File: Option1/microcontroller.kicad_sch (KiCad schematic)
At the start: 15 parts, among them U801 ESP32-WROOM-32E-N4, U802 MCP23017_SO

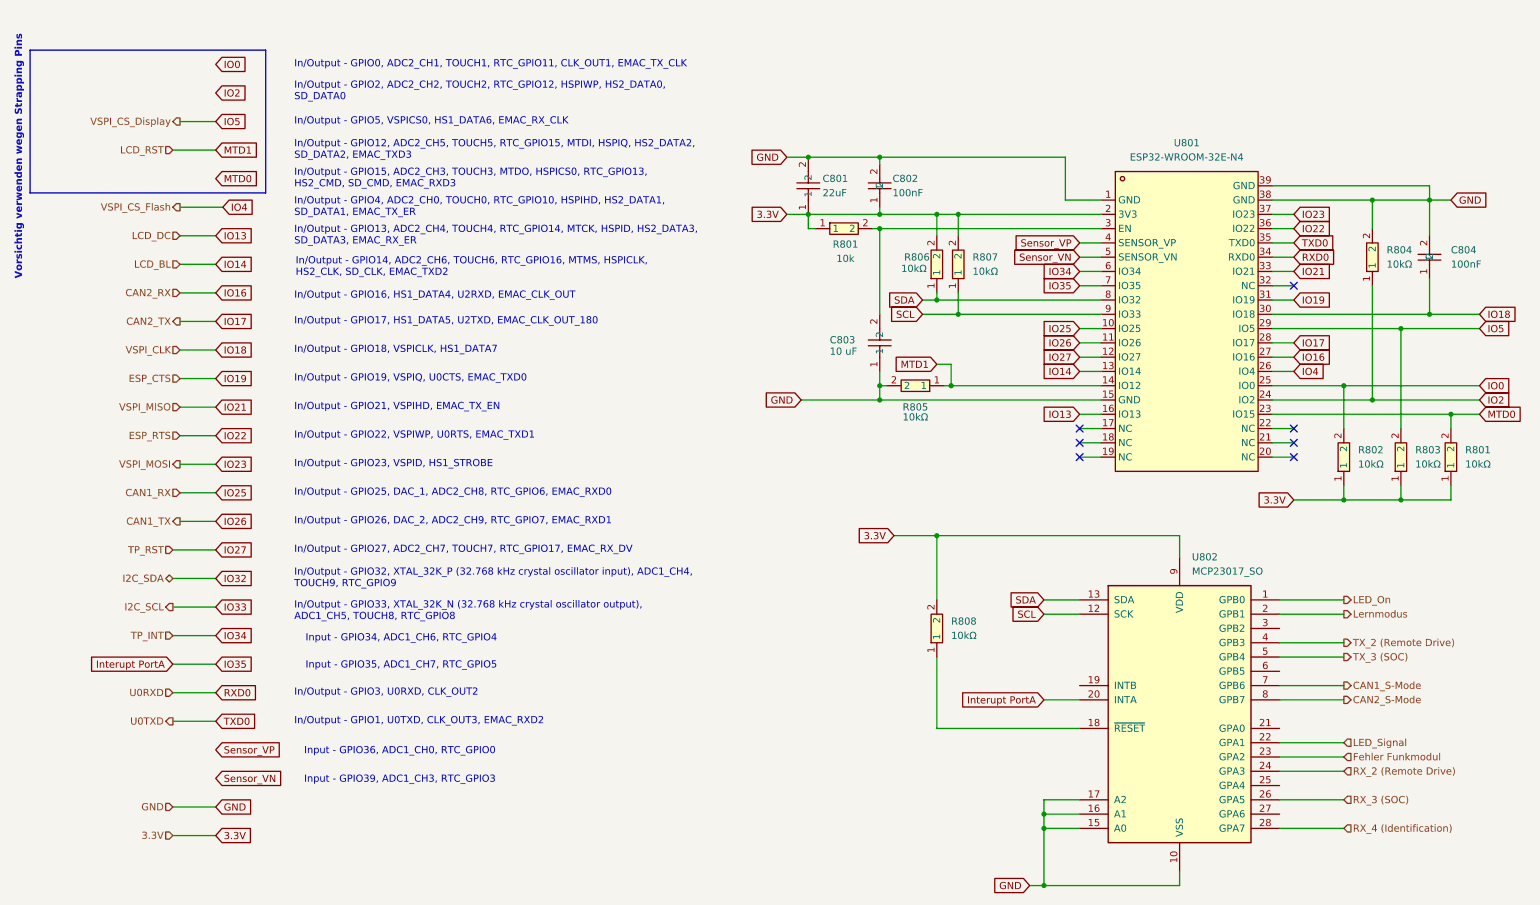
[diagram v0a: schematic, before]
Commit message: SPI Flash hinzugefügt, IN/Outputs vereinheitlicht, USB Flash Möglichkeit hinzugefügt, Display fehtl noch
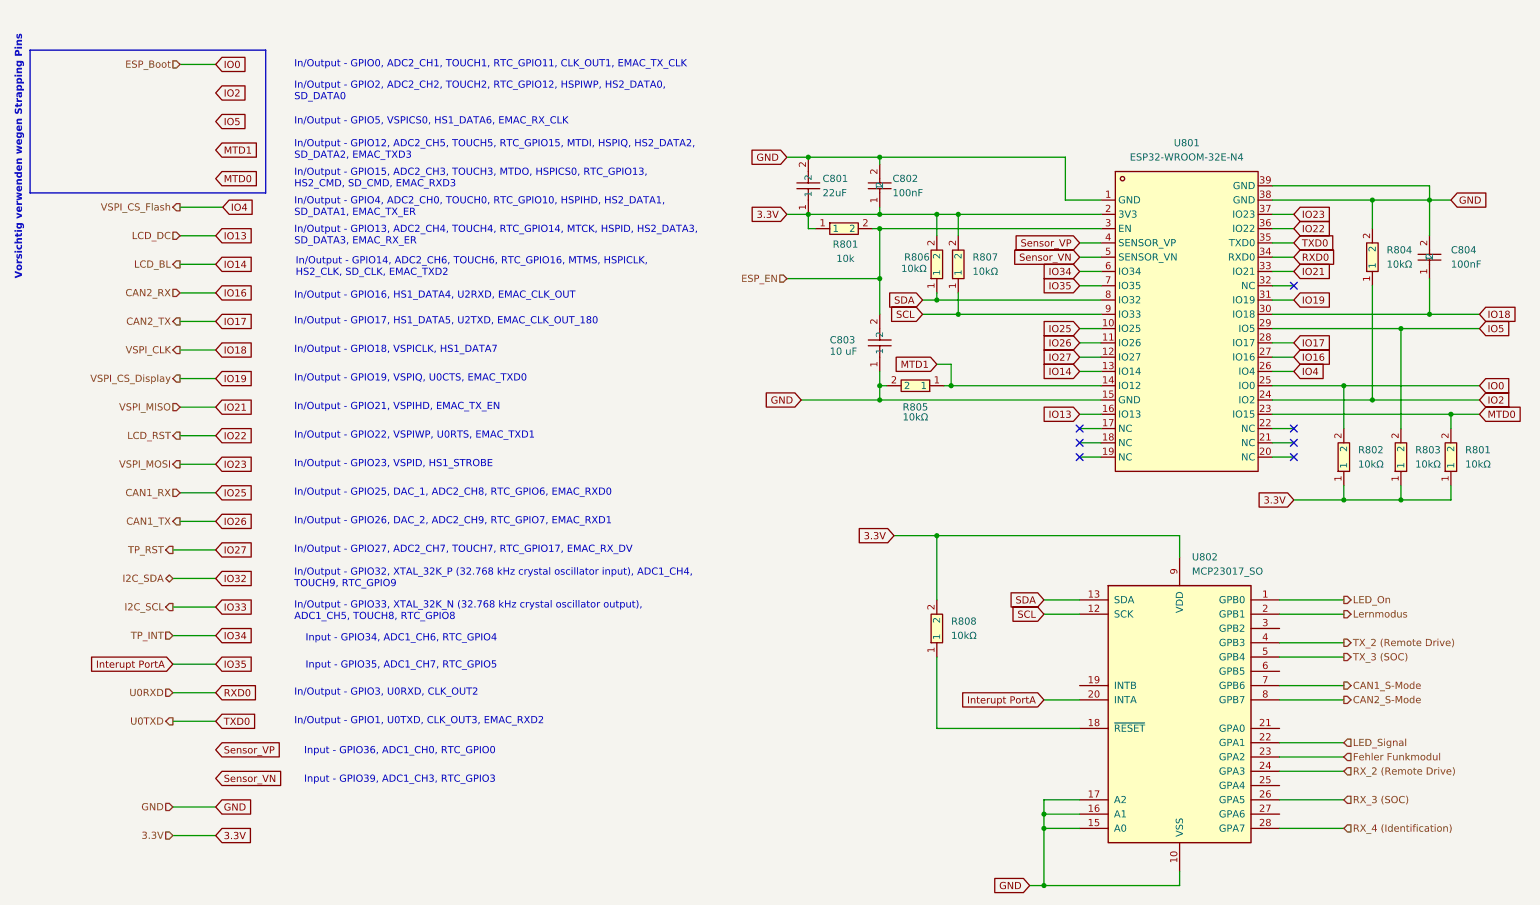
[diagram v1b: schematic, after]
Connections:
- net ESP_EN: now reaches C803.2, R801.2, U801.3 (EN)

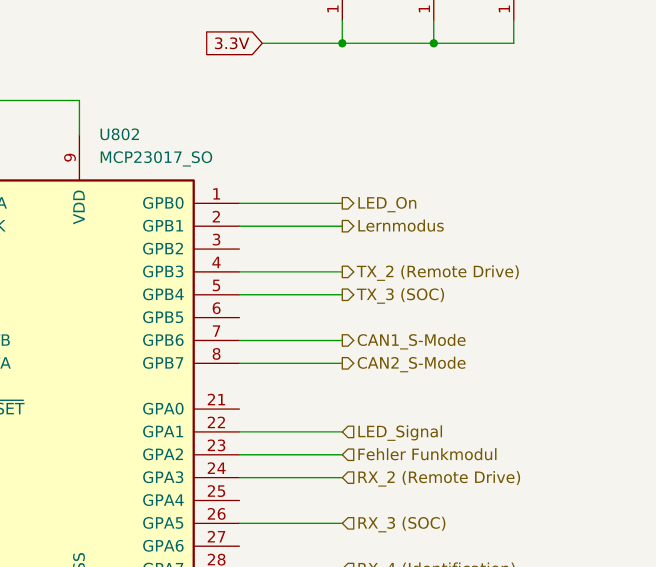
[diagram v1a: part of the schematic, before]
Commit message: USB auf 3V3 umgebaut
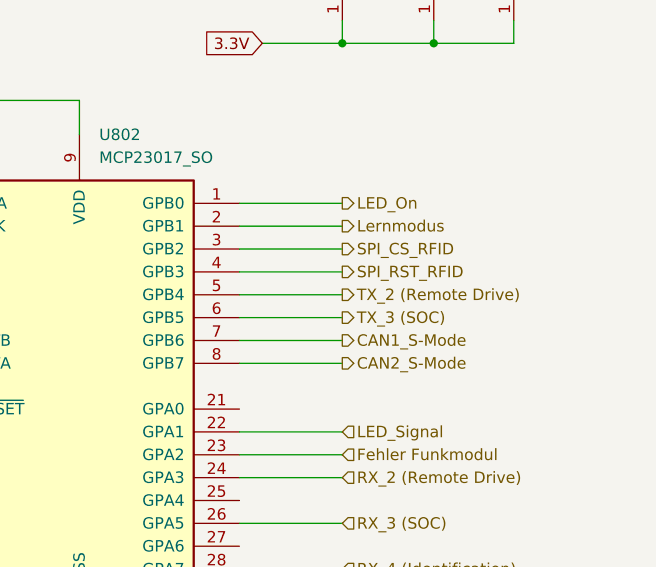
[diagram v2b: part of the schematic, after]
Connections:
- net TX_2 (Remote Drive): now also U802.5 (GPB4); no longer U802.4 (GPB3)
- net TX_3 (SOC): now also U802.6 (GPB5); no longer U802.5 (GPB4)
- net SPI_CS_RFID: now reaches U802.3 (GPB2)
- new net SPI_RST_RFID: U802.4 (GPB3)
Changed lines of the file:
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@@
 	(wire
 		(pts
+			(xy 238.76 120.65) (xy 250.19 120.65)
+		)
+		(stroke
+			(width 0)
+			(type default)
+		)
+	)
+	(wire
+		(pts
 			(xy 203.2 82.55) (xy 207.01 82.55)
 		)
@@
 	(wire
 		(pts
+			(xy 238.76 118.11) (xy 250.19 118.11)
+		)
+		(stroke
+			(width 0)
+			(type default)
+		)
+	)
+	(wire
+		(pts
 			(xy 177.8 71.12) (xy 180.34 71.12)
 		)
@@
 	(wire
 		(pts
-			(xy 238.76 120.65) (xy 250.19 120.65)
+			(xy 255.27 41.91) (xy 255.27 46.99)
 		)
 		(stroke
@@
 	(wire
 		(pts
-			(xy 255.27 41.91) (xy 255.27 46.99)
+			(xy 237.49 44.45) (xy 241.3 44.45)
 		)
 		(stroke
@@
 	(wire
 		(pts
-			(xy 237.49 44.45) (xy 241.3 44.45)
+			(xy 250.19 95.25) (xy 260.35 95.25)
 		)
 		(stroke
@@
 	(wire
 		(pts
-			(xy 250.19 95.25) (xy 260.35 95.25)
+			(xy 238.76 140.97) (xy 250.19 140.97)
 		)
 		(stroke
@@
 	(wire
 		(pts
-			(xy 238.76 140.97) (xy 250.19 140.97)
+			(xy 180.34 71.12) (xy 180.34 74.93)
 		)
 		(stroke
@@
 	(wire
 		(pts
-			(xy 180.34 71.12) (xy 180.34 74.93)
+			(xy 43.18 53.34) (xy 49.53 53.34)
 		)
 		(stroke
@@
 	(wire
 		(pts
-			(xy 43.18 53.34) (xy 49.53 53.34)
+			(xy 255.27 57.15) (xy 255.27 77.47)
 		)
 		(stroke
@@
 	(wire
 		(pts
-			(xy 255.27 57.15) (xy 255.27 77.47)
+			(xy 238.76 123.19) (xy 250.19 123.19)
 		)
 		(stroke
@@
 	(wire
 		(pts
-			(xy 238.76 123.19) (xy 250.19 123.19)
-		)
-		(stroke
-			(width 0)
-			(type default)
-		)
-	)
-	(wire
-		(pts
 			(xy 255.27 77.47) (xy 274.32 77.47)
 		)
@@
 	(wire
 		(pts
+			(xy 238.76 125.73) (xy 250.19 125.73)
+		)
+		(stroke
+			(width 0)
+			(type default)
+		)
+	)
+	(wire
+		(pts
 			(xy 237.49 46.99) (xy 241.3 46.99)
 		)
@@
 		)
 	)
+	(hierarchical_label "SPI_RST_RFID"
+		(shape output)
+		(at 250.19 120.65 0)
+		(effects
+			(font
+				(size 1.27 1.27)
+			)
+			(justify left)
+		)
+	)
 	(hierarchical_label "I2C_SDA"
 		(shape bidirectional)
@@
 		)
 	)
+	(hierarchical_label "SPI_CS_RFID"
+		(shape output)
+		(at 250.19 118.11 0)
+		(effects
+			(font
+				(size 1.27 1.27)
+			)
+			(justify left)
+		)
+	)
 	(hierarchical_label "CAN1_S-Mode"
 		(shape output)
@@
 	(hierarchical_label "TX_2 (Remote Drive)"
 		(shape output)
-		(at 250.19 120.65 0)
+		(at 250.19 123.19 0)
 		(effects
 			(font
@@
 	(hierarchical_label "TX_3 (SOC)"
 		(shape output)
-		(at 250.19 123.19 0)
+		(at 250.19 125.73 0)
 		(effects
 			(font

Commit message: Erste issues eingearbeitet
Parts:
- removed C804: 100nF, easyeda2kicad:C0603, symbol easyeda2kicad:CL10B104KA8NNNC
- removed R806, R807: 10kΩ, easyeda2kicad:R0603, symbol easyeda2kicad:0603WAF1002T5E
- added C805: 100nF, easyeda2kicad:C0603, symbol easyeda2kicad:CL10B104KA8NNNC
- added R806, R807: 4.7kΩ, easyeda2kicad:R0603, symbol EasyEda2KiCad:0603WAF4701T5E
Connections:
- net 3.3V: now also C805.1, R806.2, R807.2
- net GND: now also C805.2
- net SCL: now also R807.1
- net SDA: now also R806.1
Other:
- moved on the sheet: C801, C802, C803, R801, R802, R803, R804, R805, R808, U801, U802

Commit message: USB Schaltung angepasst, Transistoren korrigiert, Stecker ausgetauscht, Dioden hinzugefügt
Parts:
- renumbered R801 to R809
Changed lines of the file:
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@@
 	(wire
 		(pts
+			(xy 43.18 22.86) (xy 49.53 22.86)
+		)
+		(stroke
+			(width 0)
+			(type default)
+		)
+	)
+	(wire
+		(pts
 			(xy 43.18 43.18) (xy 50.8 43.18)
 		)
@@
 		)
 	)
+	(hierarchical_label "ESP_Boot2"
+		(shape input)
+		(at 43.18 22.86 180)
+		(effects
+			(font
+				(size 1.27 1.27)
+				(color 255 0 0 1)
+			)
+			(justify right)
+		)
+	)
 	(hierarchical_label "VSPI_MOSI"
 		(shape output)
@@
 		(on_board yes)
 		(dnp no)
-		(property "Reference" "R801"
+		(property "Reference" "R809"
 			(at 161.544 35.814 0)
 			(effects
@@
 			(project ""
 				(path "/b9e5f262-9648-4b79-bdd1-af888b822329/a426bcde-d9ce-4e9f-9f44-1267601fc8f5"
-					(reference "R801")
+					(reference "R809")
 					(unit 1)
 				)

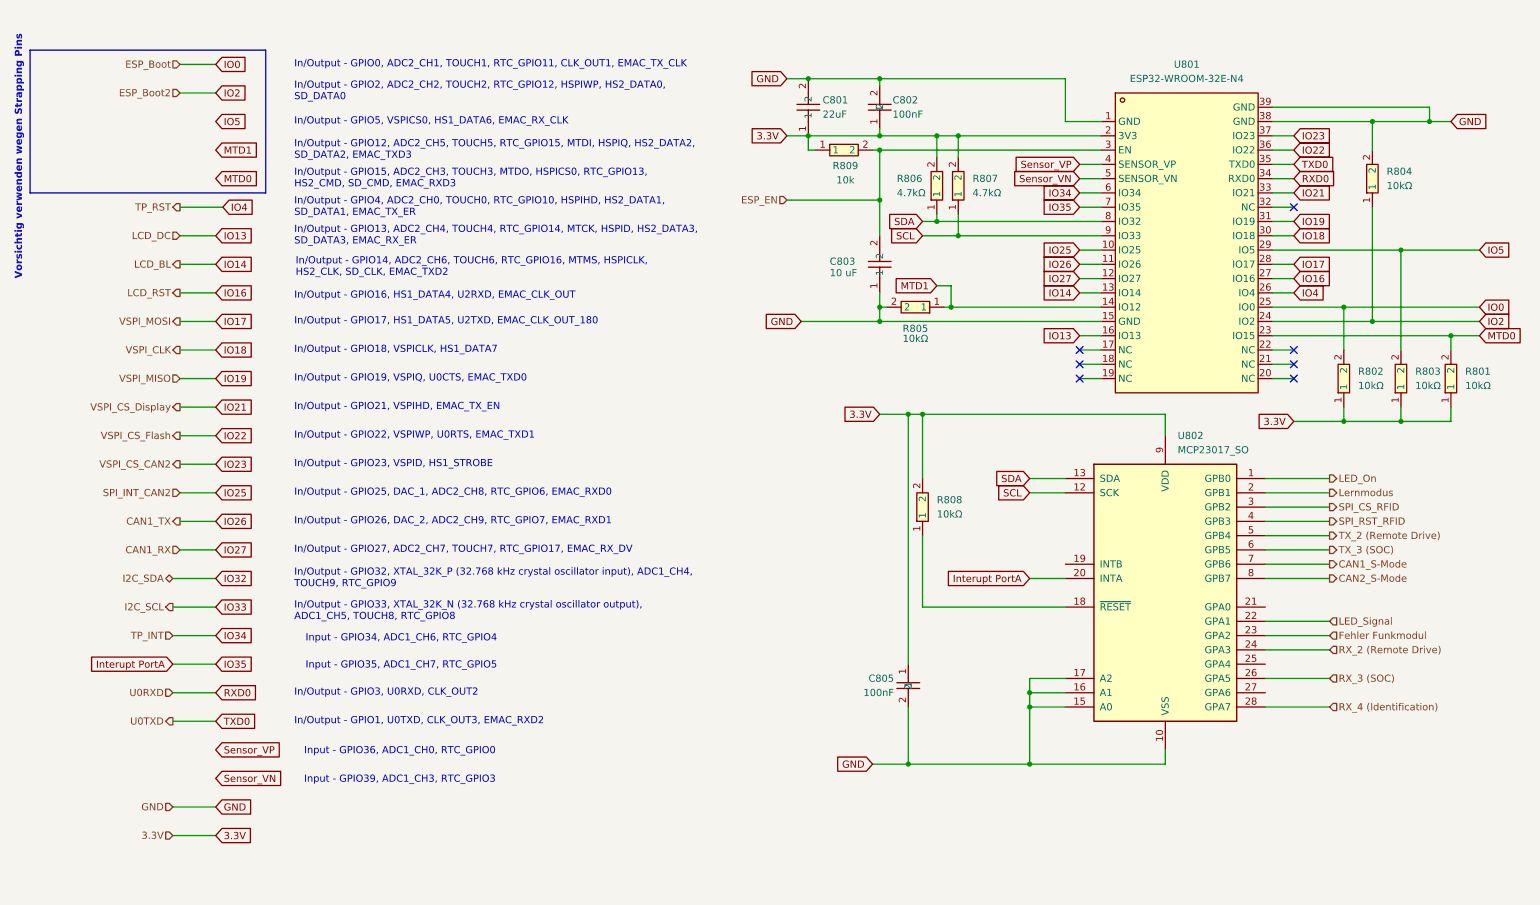
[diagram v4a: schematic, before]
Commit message: MCT und SPI zu Layout hinzugefügt
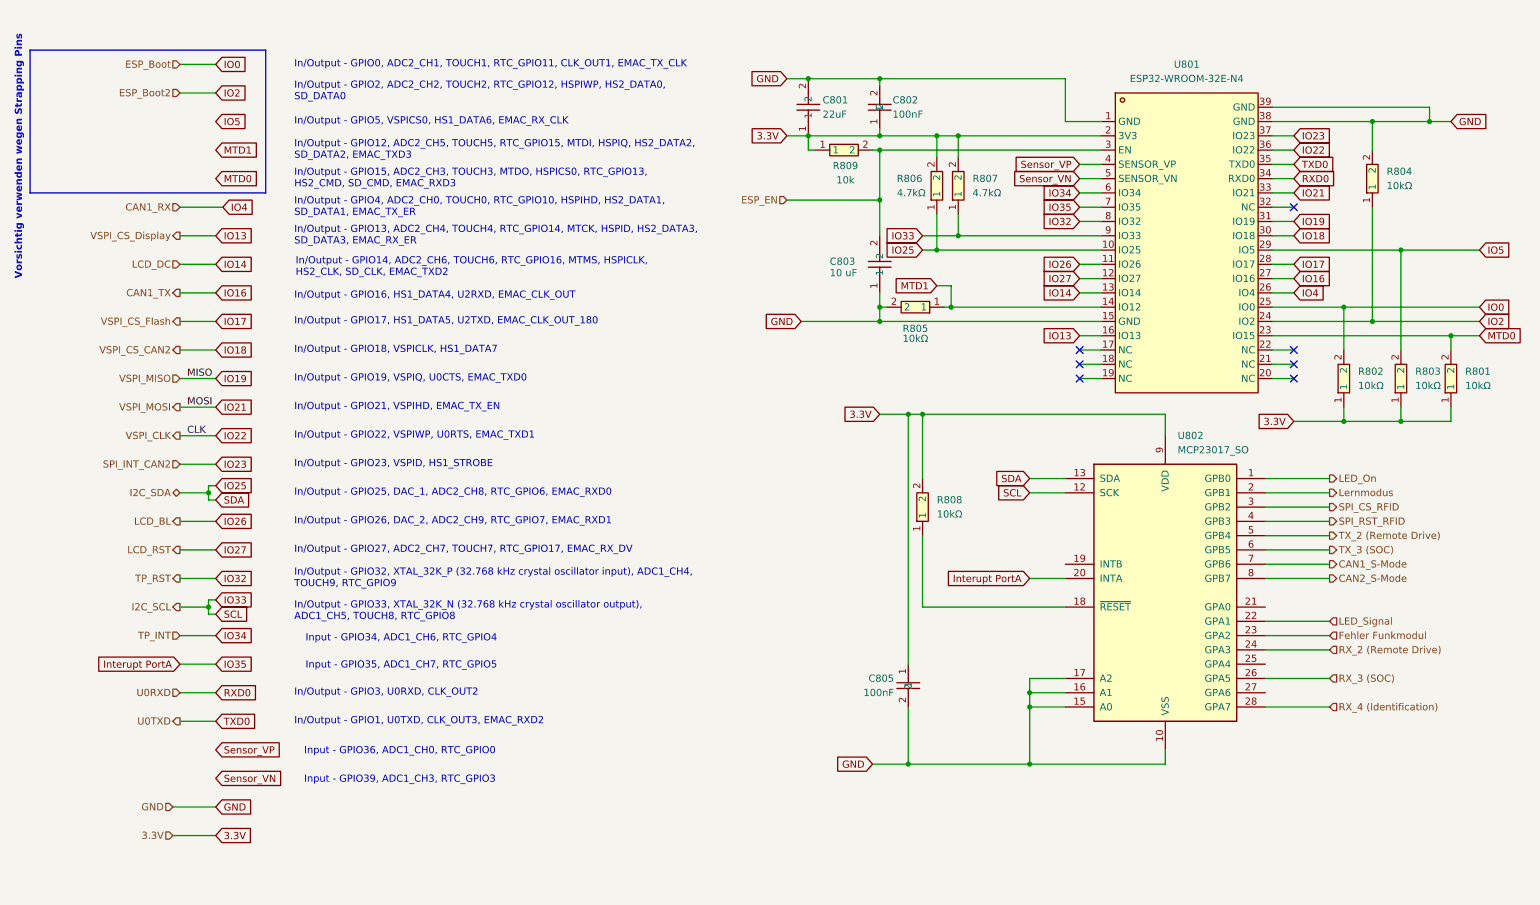
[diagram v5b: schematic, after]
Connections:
- net SCL is gone; now on net IO33: R807.1, U801.9 (IO33), U802.12 (SCK)
- net IO25: now also R806.1, U802.13 (SDA)
- net IO32: now also U801.8 (IO32)
- removed net SDA: R806.1, U801.8 (IO32), U802.13 (SDA)
